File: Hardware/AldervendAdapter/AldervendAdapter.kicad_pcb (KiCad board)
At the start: 2 copper layers, 85 x 60 mm, 42 parts, among them J101 MDB_MASTER, J102 MDB_SLAVE, J103 PROG, SW101 RESET, SW102 BOOT, U101 PC817, U102 PC817, U103 K7805M-1000R3, U104 AMS1117-3.3, U106 ESP32-C6-MINI-1

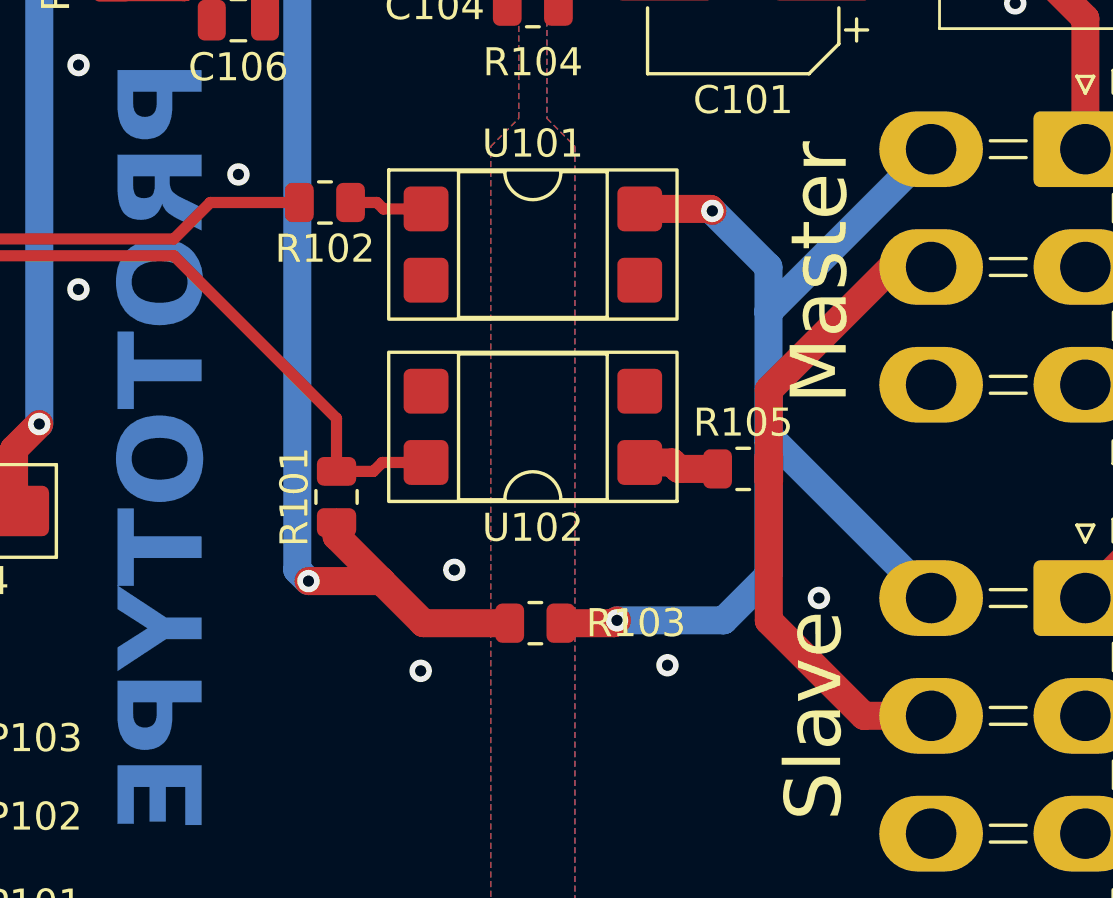
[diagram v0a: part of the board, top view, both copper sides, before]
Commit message: Fix manufacturing width for iso
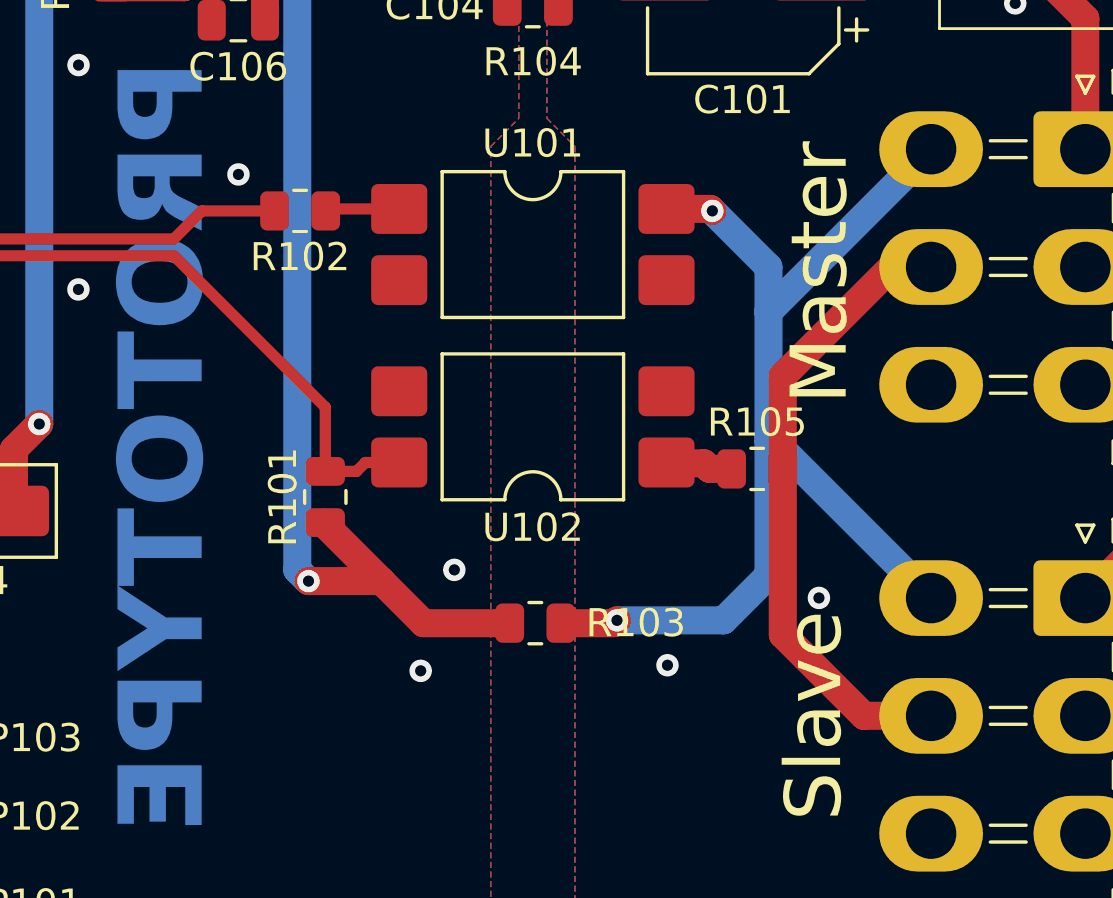
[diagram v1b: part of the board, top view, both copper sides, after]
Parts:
- U101, U102: footprint Package_DIP:DIP-4_W7.62mm_SMDSocket_SmallPads -> Package_DIP:SMDIP-4_W9.53mm
- moved R102 0.94 mm to (182.7, 89.8)
- moved R105 0.50 mm to (199.0, 99.0)
- moved R101 0.40 mm to (183.6, 100.0)
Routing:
- net Net-(R105-Pad1): track 2.87 -> 1.71 mm
- net /UART_TX: track 34.4 -> 33.4 mm
- net /MDB_RXD: track 40.9 -> 39.9 mm
- net /UART_RX: track 41.7 -> 41.0 mm

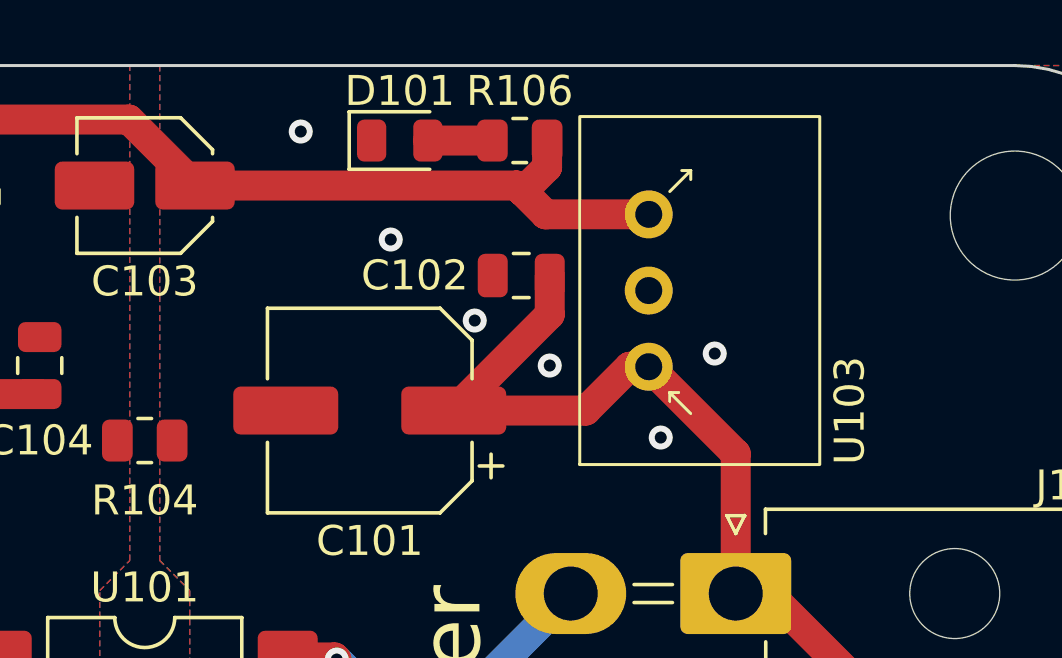
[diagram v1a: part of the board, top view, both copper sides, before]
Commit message: Fix component direction
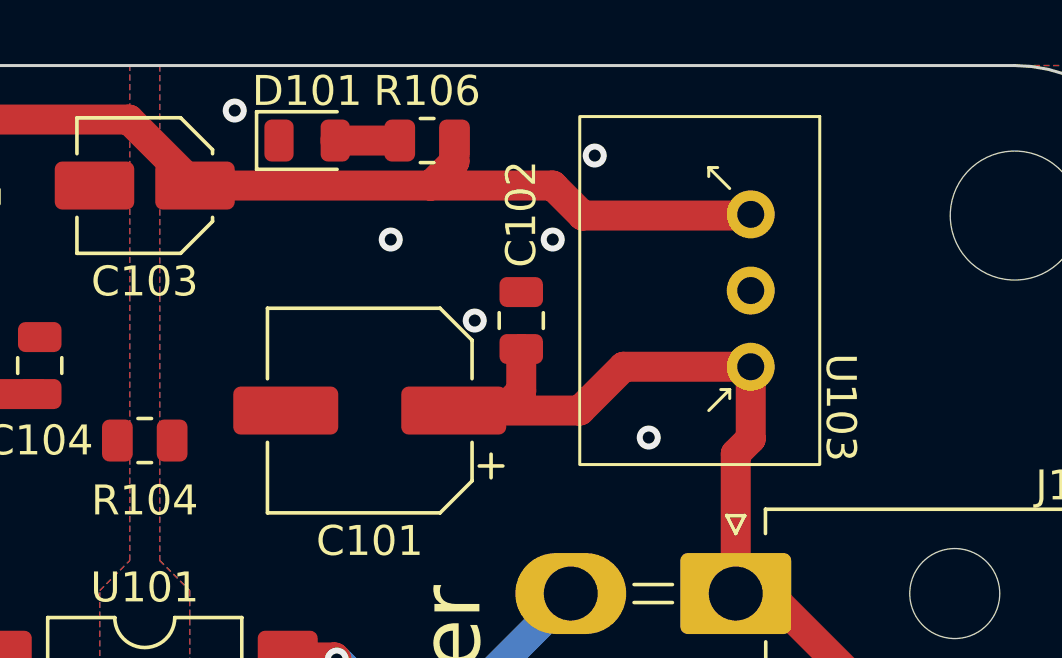
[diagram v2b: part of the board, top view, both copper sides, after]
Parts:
- moved D101 3.09 mm to (196.4, 72.5)
- moved R106 3.09 mm to (200.4, 72.5)
- moved C102 1.50 mm to (203.6, 78.5), turned to 90 degrees
- turned U103 to -90 degrees
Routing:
- net +5V: track 69.4 -> 72.4 mm

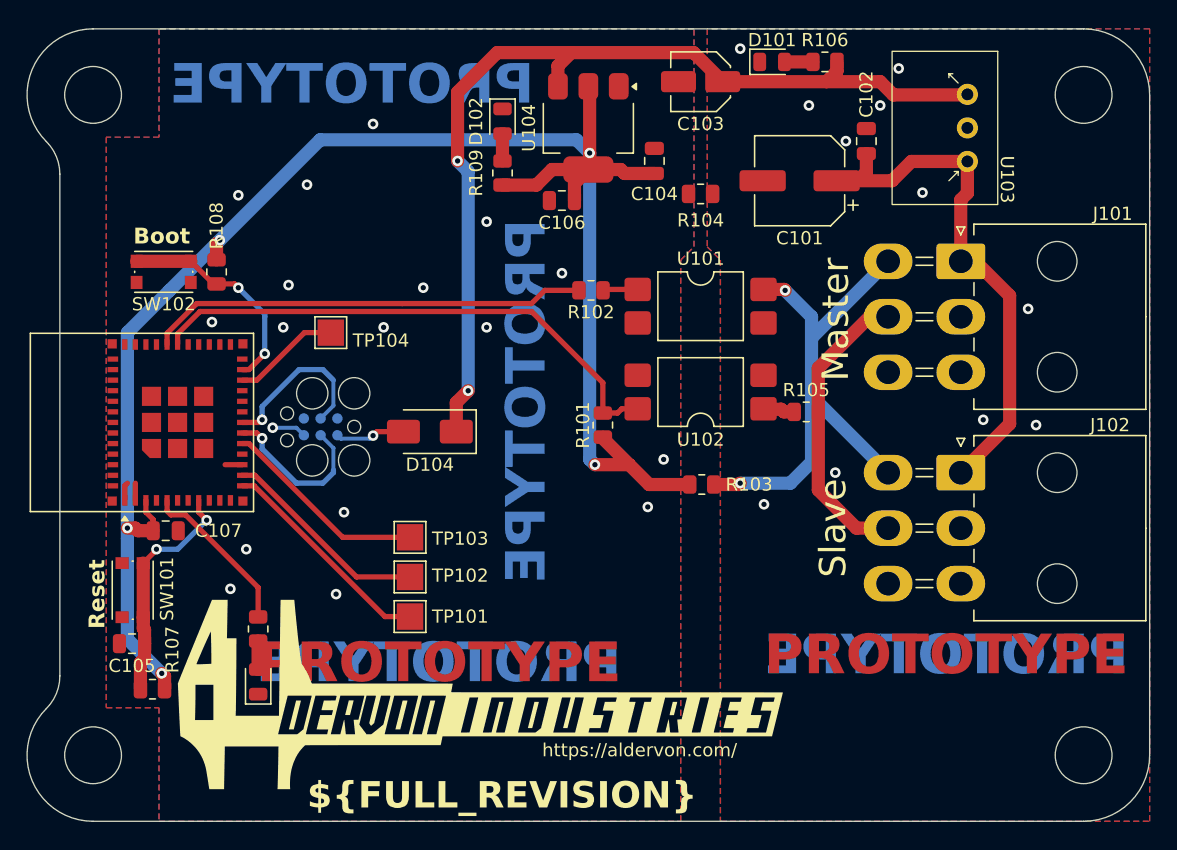
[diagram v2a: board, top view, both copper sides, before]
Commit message: Remove prototype branding
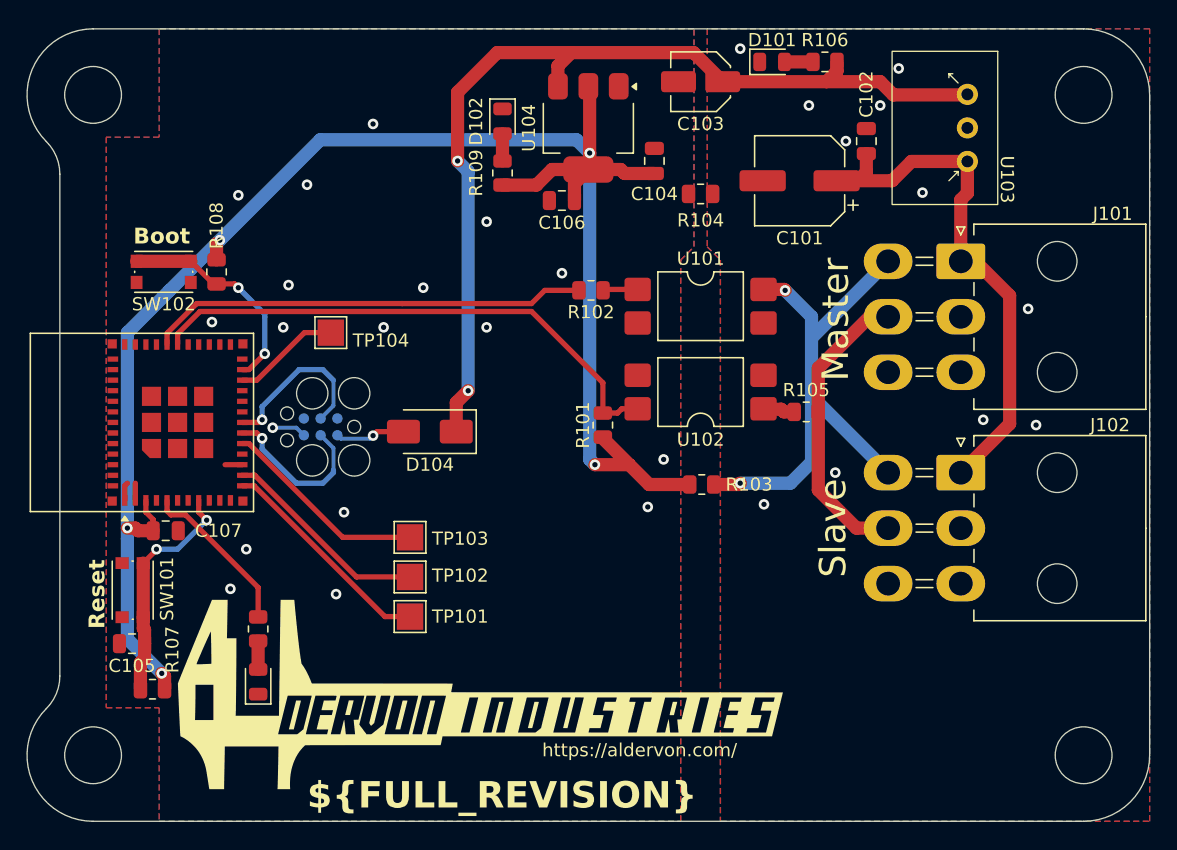
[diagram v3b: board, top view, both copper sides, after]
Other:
- board text removed: "PROTOTYPE"
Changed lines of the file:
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@@
 		(layer "Edge.Cuts")
-	)
-	(gr_text "PROTOTYPE"
-		(at 209.6 117.4 0)
-		(layer "F.Cu" knockout)
-		(effects
-			(font
-				(size 3 3)
-				(thickness 0.75)
-				(bold yes)
-			)
-		)
-	)
-	(gr_text "PROTOTYPE"
-		(at 171.2 118 0)
-		(layer "F.Cu" knockout)
-		(effects
-			(font
-				(size 3 3)
-				(thickness 0.75)
-				(bold yes)
-			)
-		)
-	)
-	(gr_text "PROTOTYPE"
-		(at 171.2 118 -0)
-		(layer "B.Cu" knockout)
-		(effects
-			(font
-				(size 3 3)
-				(thickness 0.75)
-				(bold yes)
-			)
-			(justify mirror)
-		)
-	)
-	(gr_text "PROTOTYPE"
-		(at 177.8 98.2 90)
-		(layer "B.Cu" knockout)
-		(effects
-			(font
-				(size 3 3)
-				(thickness 0.75)
-				(bold yes)
-			)
-			(justify mirror)
-		)
-	)
-	(gr_text "PROTOTYPE"
-		(at 209.6 117.4 -0)
-		(layer "B.Cu" knockout)
-		(effects
-			(font
-				(size 3 3)
-				(thickness 0.75)
-				(bold yes)
-			)
-			(justify mirror)
-		)
-	)
-	(gr_text "PROTOTYPE"
-		(at 164.6 74.2 -0)
-		(layer "B.Cu" knockout)
-		(effects
-			(font
-				(size 3 3)
-				(thickness 0.75)
-				(bold yes)
-			)
-			(justify mirror)
-		)
 	)
 	(gr_text "Slave"
